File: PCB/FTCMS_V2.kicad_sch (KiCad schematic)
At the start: 113 parts, among them J1 Conn_01x20_Female, J2 Conn_02x10_Odd_Even, J3 ToSlave, J4 Conn_02x02_Odd_Even, J6 ToMaster, Q1 Q_NPN_BCE DZT5551, U1 ADBMS1818ASWAZ, U2 MAX9031AU

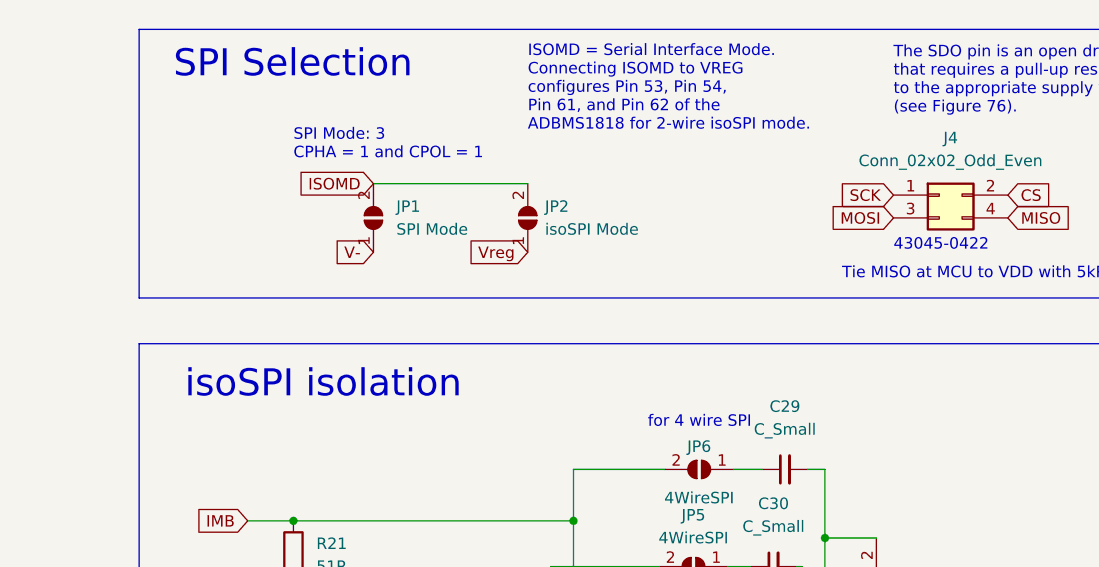
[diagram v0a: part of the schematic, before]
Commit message: seems to work, no more pec error. Used 10k pullup between miso and vdd 5V arduino
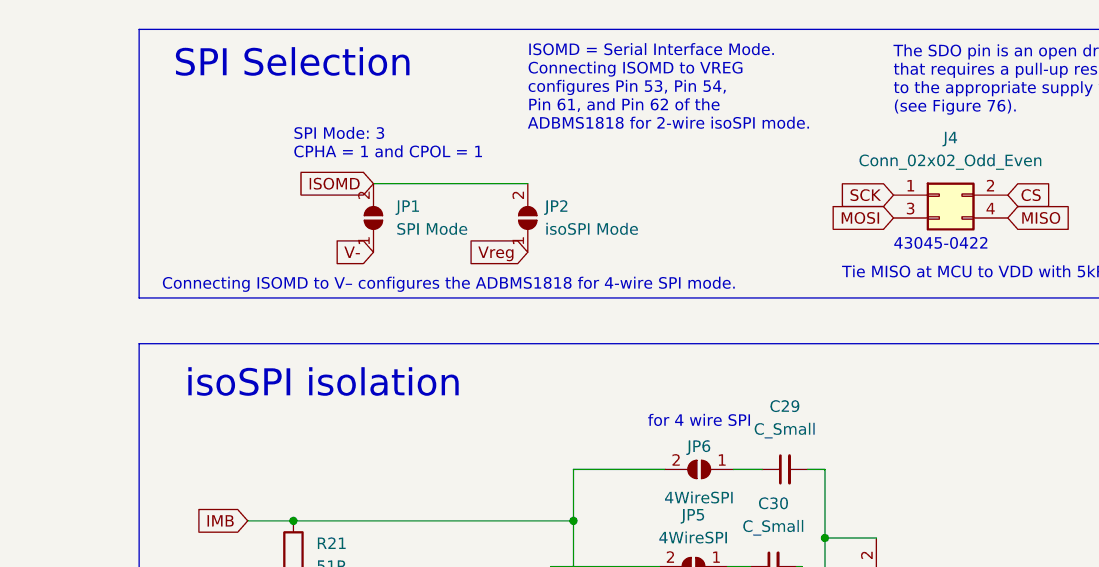
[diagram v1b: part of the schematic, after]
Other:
- note added: "Connecting ISOMD to V– configures the ADBMS1818 for 4-wire SPI mode."
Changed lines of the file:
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@@
     (effects (font (size 3 3)) (justify left bottom))
+  )
+  (text "Connecting ISOMD to V– configures the ADBMS1818 for 4-wire SPI mode."
+    (at 280.035 127 0)
+    (effects (font (size 1.27 1.27)) (justify left bottom))
   )
   (text "Fragen" (at 32.766 192.913 0)
